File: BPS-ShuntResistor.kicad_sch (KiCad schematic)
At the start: 11 parts, among them J3 Amp_Conn

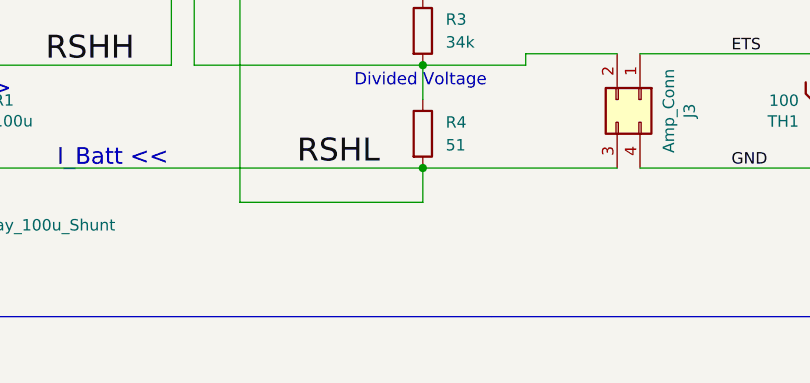
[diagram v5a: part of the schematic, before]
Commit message: resistor placement change
make tracks more readable + add some text for pins
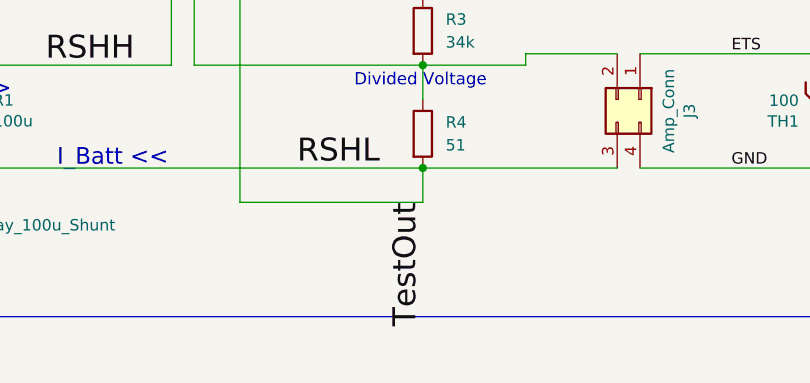
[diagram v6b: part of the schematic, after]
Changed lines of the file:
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@@
     (effects (font (size 2.54 2.54)) (justify left bottom))
+  )
+  (label "TestOut" (at 153.67 121.92 270)
+    (effects (font (size 2.54 2.54)) (justify right bottom))
   )
   (global_label "RSHL" (shape input) (at 199.39 81.28 270) (fields_autoplaced)
@@
     )
     (path "/4f59afea-52a6-42ef-a827-b3f6d4652563"
-      (reference "CurrentBoardConn1") (unit 1) (value "Conn_01x05_Male") (footprint "Connector_PinHeader_2.54mm:PinHeader_1x05_P2.54mm_Vertical_SMD_Pin1Left")
+      (reference "CurrentBoardConn1") (unit 1) (value "Conn_01x05_Male") (footprint "Connector_PinHeader_2.54mm:PinHeader_1x05_P2.54mm_Vertical")
     )
     (path "/00000000-0000-0000-0000-00005f6f5e19"
@@
     )
     (path "/46651b6a-aae7-4589-85a3-9dbcf0861909"
-      (reference "ShuntTestJumper1") (unit 1) (value "Conn_01x05_Male") (footprint "Connector_PinHeader_2.54mm:PinHeader_1x05_P2.54mm_Vertical_SMD_Pin1Left")
+      (reference "ShuntTestJumper1") (unit 1) (value "Conn_01x05_Male") (footprint "Connector_PinHeader_2.54mm:PinHeader_1x05_P2.54mm_Vertical")
     )
     (path "/bff0be5b-fcea-4d1b-a22e-58c65723f733"
